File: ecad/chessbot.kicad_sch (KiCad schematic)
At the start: 1 part, among them J1 ESP32-PICO-KIT

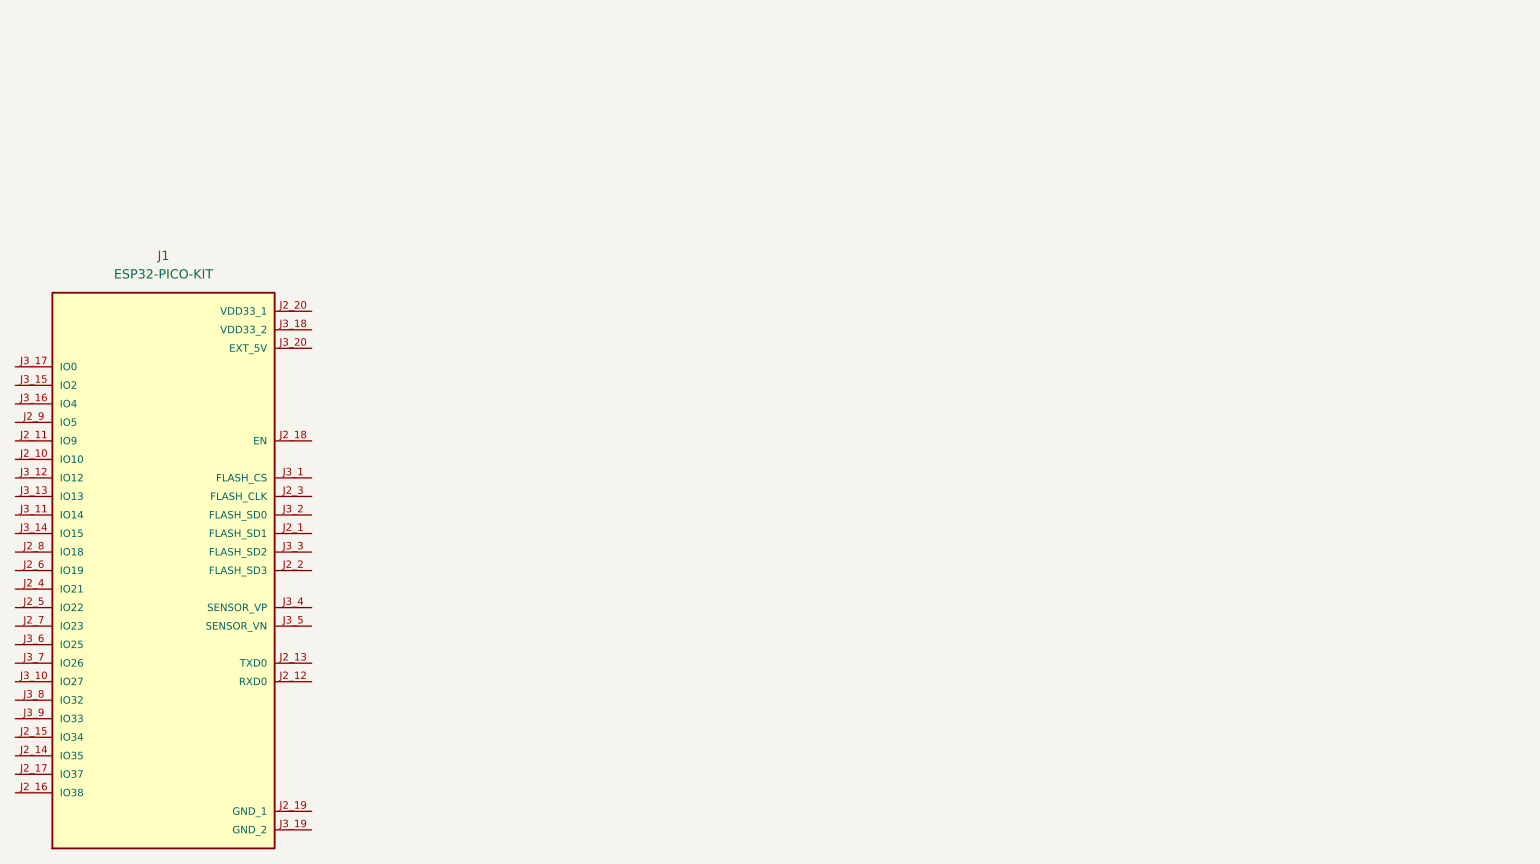
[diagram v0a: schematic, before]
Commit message: lay out chess board sensors + leds
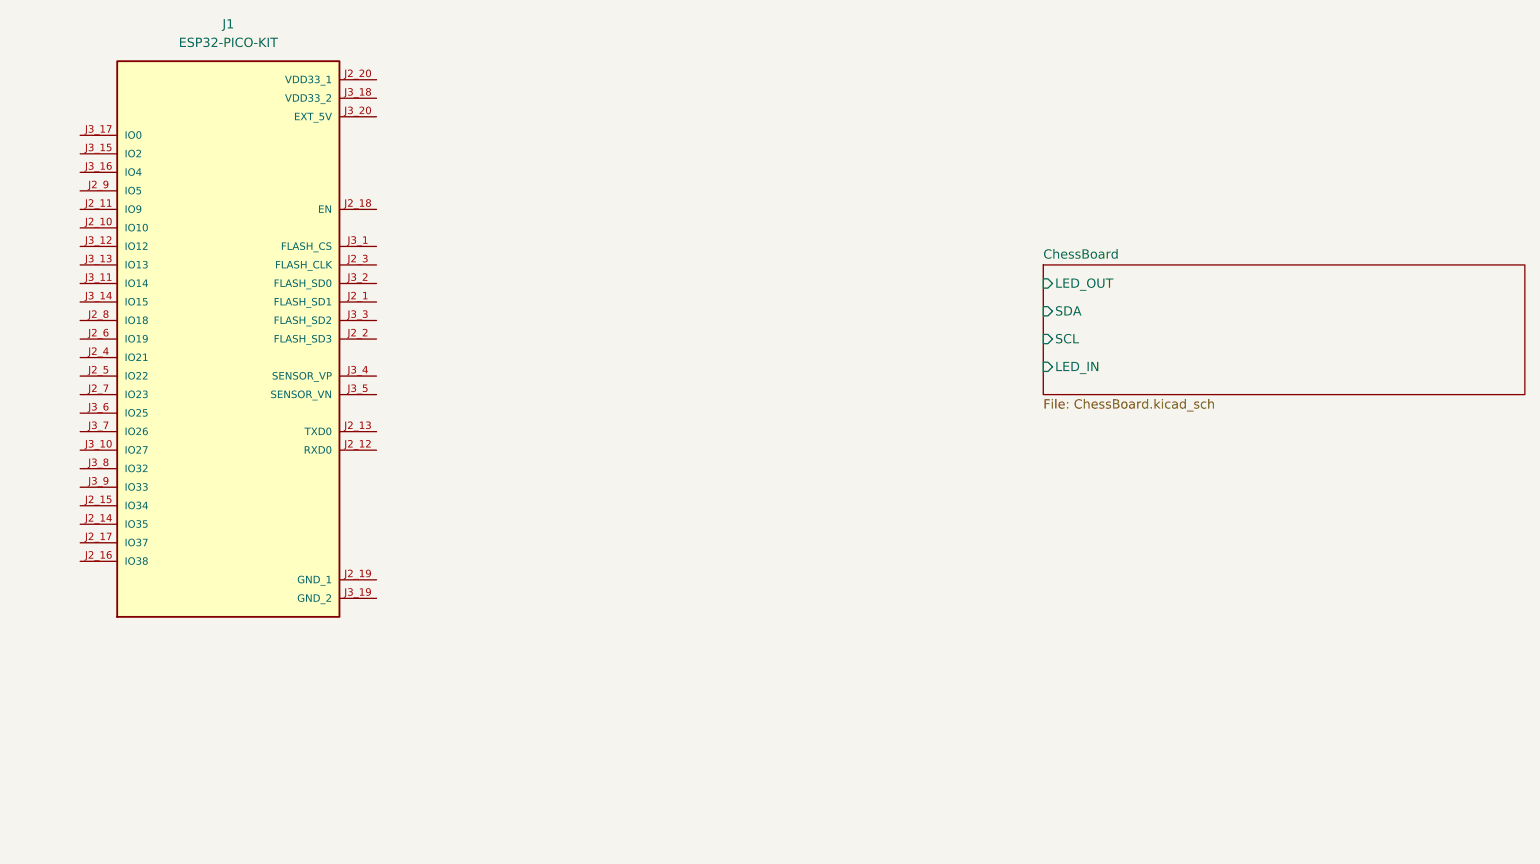
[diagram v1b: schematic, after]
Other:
- added sheet ChessBoard (ChessBoard.kicad_sch)
- moved on the sheet: J1
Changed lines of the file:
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@@
 (kicad_sch (version 20230121) (generator eeschema)
   (paper "A4")
-  (symbol (lib_id "esp32-pico-kit:ESP32-PICO-KIT") (at 74.93 125.73 0) (unit 1)
+  (symbol (lib_id "esp32-pico-kit:ESP32-PICO-KIT") (at 83.82 93.98 0) (unit 1)
     (in_bom yes) (on_board yes) (dnp no) (fields_autoplaced)
-    (property "Reference" "J1" (at 74.93 82.55 0)
+    (property "Reference" "J1" (at 83.82 50.8 0)
       (effects (font (size 1.27 1.27)))
     )
-    (property "Value" "ESP32-PICO-KIT" (at 74.93 85.09 0)
+    (property "Value" "ESP32-PICO-KIT" (at 83.82 53.34 0)
       (effects (font (size 1.27 1.27)))
     )
-    (property "Footprint" "ESP32-PICO-KIT:XCVR_ESP32-PICO-KIT" (at 74.93 125.73 0)
+    (property "Footprint" "ESP32-PICO-KIT:XCVR_ESP32-PICO-KIT" (at 83.82 93.98 0)
       (effects (font (size 1.27 1.27)) (justify bottom) hide)
     )
-    (property "Datasheet" "" (at 74.93 125.73 0)
+    (property "Datasheet" "" (at 83.82 93.98 0)
       (effects (font (size 1.27 1.27)) hide)
     )
-    (property "PARTREV" "4.1" (at 74.93 125.73 0)
+    (property "PARTREV" "4.1" (at 83.82 93.98 0)
       (effects (font (size 1.27 1.27)) (justify bottom) hide)
     )
-    (property "DESCRIPTION" "Esp32 Wifi Bluetooth Eval Board" (at 74.93 125.73 0)
+    (property "DESCRIPTION" "Esp32 Wifi Bluetooth Eval Board" (at 83.82 93.98 0)
       (effects (font (size 1.27 1.27)) (justify bottom) hide)
     )
-    (property "MANUFACTURER" "Espressif Systems" (at 74.93 125.73 0)
+    (property "MANUFACTURER" "Espressif Systems" (at 83.82 93.98 0)
       (effects (font (size 1.27 1.27)) (justify bottom) hide)
     )
@@
       )
     )
+  )
+  (sheet (at 195.58 83.82) (size 66.04 17.78) (fields_autoplaced)
+    (stroke (width 0.1524) (type solid))
+    (fill (color 0 0 0 0.0000))
+    (property "Sheetname" "ChessBoard" (at 195.58 83.1084 0)
+      (effects (font (size 1.27 1.27)) (justify left bottom))
+    )
+    (property "Sheetfile" "ChessBoard.kicad_sch" (at 195.58 102.1846 0)
+      (effects (font (size 1.27 1.27)) (justify left top))
+    )
+    (pin "LED_OUT" input (at 195.58 86.36 180)
+      (effects (font (size 1.27 1.27)) (justify left))
+    )
+    (pin "SDA" input (at 195.58 90.17 180)
+      (effects (font (size 1.27 1.27)) (justify left))
+    )
+    (pin "SCL" input (at 195.58 93.98 180)
+      (effects (font (size 1.27 1.27)) (justify left))
+    )
+    (pin "LED_IN" input (at 195.58 97.79 180)
+      (effects (font (size 1.27 1.27)) (justify left))
+    )
+    (instances
+      (project "chessbot"
+        (path "/178674ef-da23-4447-9d4b-ea3429461404" (page "2"))
+      )
+    )
